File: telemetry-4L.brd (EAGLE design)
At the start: 69.8 x 22.9 mm, 70 parts, among them SW1 MF-SW-TACT-4.2MM, SW2 SWITCH_SPDT, U1 ATSAMD21G18A-MUT, U2 SPX3819M5-L-3-0, U3 MCP73831T-2ACI/OT, U4 DMG6968U, U5 SIM868, U6 BMP280, U7 MPU-9250, U8 TPS61253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

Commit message: Seems ok now
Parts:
- L1: value DFE322512C -> 1277AS-H-1R0M=P2
- SW2: value SWITCH_SPDT -> PCM12SMTR
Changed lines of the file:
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@@
 <layer number="25" name="tNames" color="7" fill="1" visible="yes" active="yes"/>
 <layer number="26" name="bNames" color="7" fill="1" visible="yes" active="yes"/>
-<layer number="27" name="tValues" color="7" fill="1" visible="no" active="yes"/>
-<layer number="28" name="bValues" color="7" fill="1" visible="no" active="yes"/>
+<layer number="27" name="tValues" color="7" fill="1" visible="yes" active="yes"/>
+<layer number="28" name="bValues" color="7" fill="1" visible="yes" active="yes"/>
 <layer number="29" name="tStop" color="7" fill="3" visible="yes" active="yes"/>
 <layer number="30" name="bStop" color="7" fill="6" visible="yes" active="yes"/>
@@
 <attribute name="VALUE" x="64.897" y="6.1595" size="0.889" layer="28" ratio="11" rot="MR180"/>
 </element>
-<element name="SW2" library="SparkFun-Electromechanical" package="KPS-1290" value="SWITCH_SPDT" x="1.778" y="11.43" rot="MR90">
+<element name="SW2" library="SparkFun-Electromechanical" package="KPS-1290" value="PCM12SMTR" x="1.778" y="11.43" rot="MR90">
 <attribute name="PROD_ID" value="SWCH-10651" x="1.778" y="11.43" size="1.778" layer="28" rot="MR90" display="off"/>
 </element>
@@
 <attribute name="VALUE" x="50.673" y="23.1775" size="1.27" layer="28" font="vector" ratio="18" rot="MR180" align="center"/>
 </element>
-<element name="L1" library="MF_Passives" package="L1210" value="DFE322512C" x="47.6885" y="20.3835" smashed="yes" rot="MR90">
+<element name="L1" library="MF_Passives" package="L1210" value="1277AS-H-1R0M=P2" x="47.6885" y="20.3835" smashed="yes" rot="MR90">
 <attribute name="HOUSEPART" value="" x="47.6885" y="20.3835" size="1.778" layer="28" rot="MR90" display="off"/>
 <attribute name="POPULATE" value="" x="47.6885" y="20.3835" size="1.778" layer="28" rot="MR90" display="off"/>

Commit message: fixed some names
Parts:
- U4: value DMG6968U -> IRLML6344TRPBF
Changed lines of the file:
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@@
 <element name="JP7" library="SparkFun-Passives" package="PAD-JUMPER-2-NO_YES_SILK" value="JUMPER-PAD-2-NOYES_SILK" x="4.572" y="7.62" rot="MR0"/>
 <element name="JP8" library="SparkFun-Passives" package="PAD-JUMPER-2-NC_BY_TRACE_YES_SILK" value="JUMPER-PAD-2-NC_BY_TRACE" x="4.572" y="15.24" rot="MR0"/>
-<element name="U4" library="MF_Discrete_Semiconductor" package="SOT-23-3" value="DMG6968U" x="66.421" y="16.002" smashed="yes" rot="R90">
+<element name="U4" library="MF_Discrete_Semiconductor" package="SOT-23-3" value="IRLML6344TRPBF" x="66.421" y="16.002" smashed="yes" rot="R90">
 <attribute name="MPN" value="" x="66.421" y="16.002" size="1.778" layer="27" rot="R90" display="off"/>
 <attribute name="HOUSEPART" value="NO" x="66.421" y="16.002" size="1.778" layer="27" rot="R90" display="off"/>

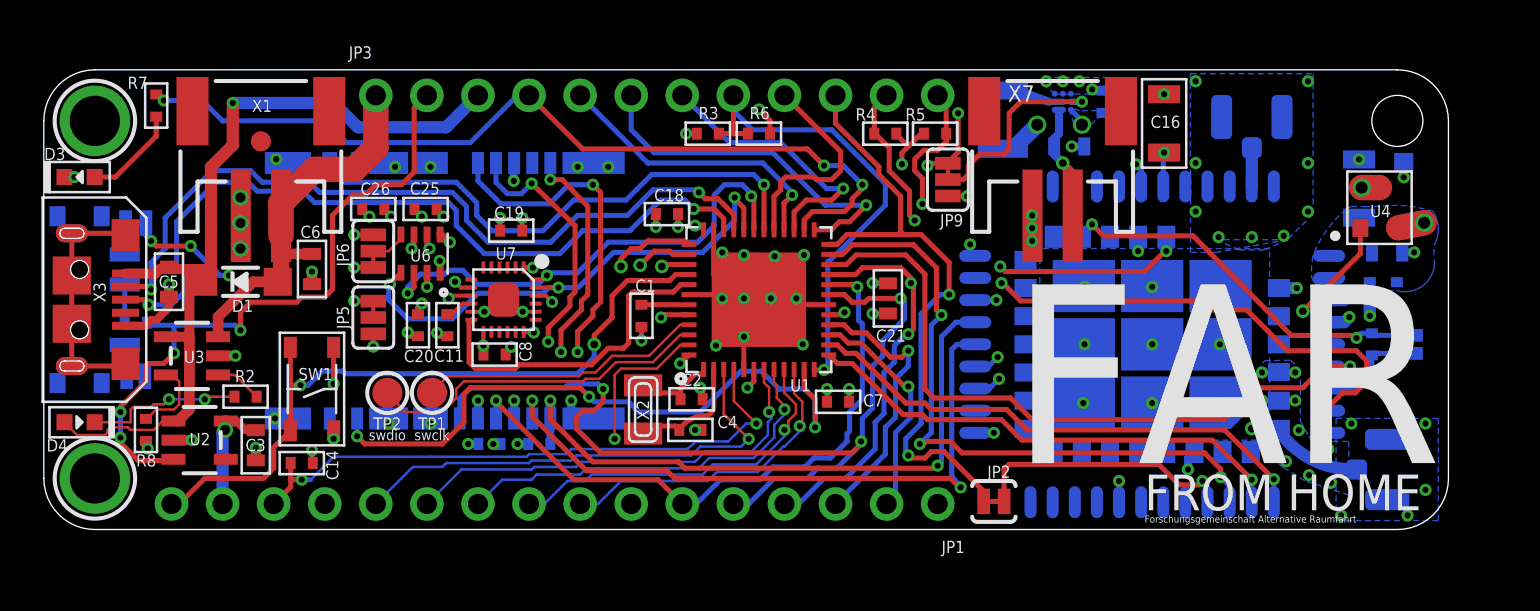
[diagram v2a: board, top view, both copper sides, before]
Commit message: Moved power mosfet back upstream
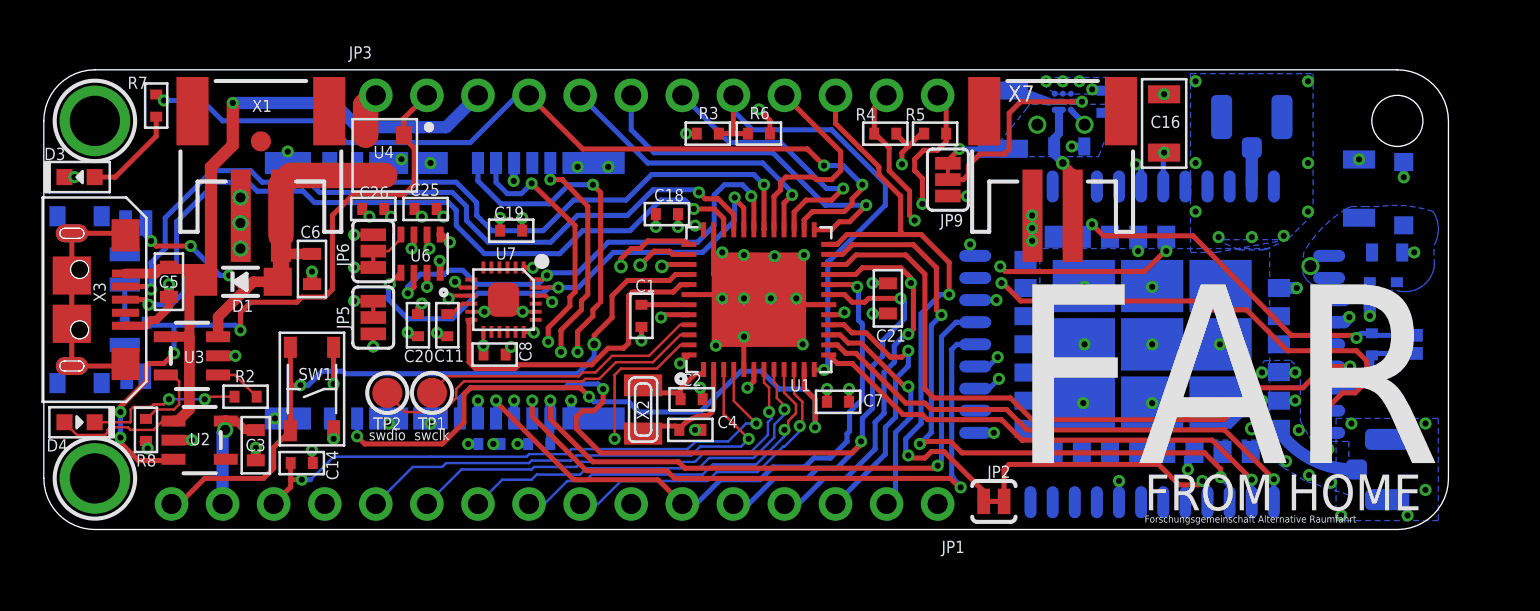
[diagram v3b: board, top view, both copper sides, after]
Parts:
- moved U4 49.5 mm to (17.0, 18.6), turned to 270 degrees
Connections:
- net EN: no longer JP9.3
- net VBAT: no longer C22.P$1, JP3.1, L1.P$1, R3.P$1, U8.A3
- net VBAT_ON: now also C22.P$1, JP3.1, JP9.3, L1.P$1, R3.P$1, U8.A3
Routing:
- net VBAT: track 92.0 -> 24.3 mm, vias 7 -> 3
- net EN: track 94.2 -> 34.7 mm, vias 7 -> 4
- net VBAT_ON: track 1.30 -> 58.0 mm, vias 1 -> 5
- net GND: track 70.5 -> 71.4 mm
- removed copper zone on layer 16, net VBAT

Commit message: tweaks
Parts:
- removed U$34: FIDUCIAL"", microbuilder:FIDUCIAL_1MM
- D3: value RED -> MF-LED-0603-RED
- D4: value GREEN -> MF-LED-0603-GREEN
- U8: value TPS61253 -> TPS61253YFFR
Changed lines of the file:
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@@
 <attribute name="VALUE" x="66.230496875" y="15.684503125" size="0.4064" layer="28" rot="MR90"/>
 </element>
-<element name="D3" library="MF_LEDs" package="LED0603" value="RED" x="1.778" y="17.526" smashed="yes">
+<element name="D3" library="MF_LEDs" package="LED0603" value="MF-LED-0603-RED" x="1.778" y="17.526" smashed="yes">
 <attribute name="MPN" value="MF-LED-0603-RED" x="1.778" y="17.526" size="1.778" layer="27" display="off"/>
 <attribute name="URL" value="https://factory.macrofab.com/part/MF-LED-0603-RED" x="1.778" y="17.526" size="1.778" layer="27" display="off"/>
@@
 <attribute name="NAME" x="0.0145" y="18.372" size="0.6096" layer="25" font="vector" ratio="18"/>
 </element>
-<element name="D4" library="MF_LEDs" package="LED0603" value="GREEN" x="1.778" y="5.334" smashed="yes" rot="R180">
+<element name="D4" library="MF_LEDs" package="LED0603" value="MF-LED-0603-GREEN" x="1.778" y="5.334" smashed="yes" rot="R180">
 <attribute name="MPN" value="MF-LED-0603-GREEN" x="1.778" y="5.334" size="1.778" layer="27" rot="R180" display="off"/>
 <attribute name="URL" value="https://factory.macrofab.com/part/MF-LED-0603-GREEN" x="1.778" y="5.334" size="1.778" layer="27" rot="R180" display="off"/>
@@
 <attribute name="BOM" value="EXCLUDE" x="2.54" y="2.54" size="1.778" layer="27" display="off"/>
 </element>
-<element name="U$34" library="microbuilder" package="FIDUCIAL_1MM" value="FIDUCIAL&quot;&quot;" x="10.795" y="19.304" smashed="yes">
-<attribute name="BOM" value="EXCLUDE" x="10.795" y="19.304" size="1.778" layer="27" display="off"/>
-</element>
 <element name="U1" library="microbuilder" package="TQFN48_7MM" value="ATSAMD21G18A-MUT" x="35.56" y="11.43" smashed="yes">
 <attribute name="NAME" x="38.1411375" y="7.4745" size="0.6096" layer="25" font="vector" ratio="18" rot="R180"/>
@@
 </element>
 <element name="X7" library="microbuilder" package="JSTPH2" value="S2B-PH-SM4-TB(LF)(SN)" x="50.165" y="19.304"/>
-<element name="U8" library="Custom" package="YFF9" value="TPS61253" x="50.673" y="21.2725" smashed="yes" rot="MR180">
+<element name="U8" library="Custom" package="YFF9" value="TPS61253YFFR" x="50.673" y="21.2725" smashed="yes" rot="MR180">
 <attribute name="COPYRIGHT" value="Copyright (C) 2015 Accelerated Designs. All rights reserved" x="50.673" y="21.2725" size="1.778" layer="28" rot="MR180" display="off"/>
 <attribute name="VENDOR" value="Texas Instruments" x="50.673" y="21.2725" size="1.778" layer="28" rot="MR180" display="off"/>
@@
 <vertex x="49.022" y="21.1455"/>
 </polygon>
-<wire x1="32.47" y1="19.685" x2="44.958" y2="18.3515" width="0" layer="19" extent="1-1"/>
 <wire x1="51.7525" y1="20.1295" x2="51.073" y2="20.8725" width="0.3048" layer="16"/>
+<wire x1="44.958" y1="18.3515" x2="32.47" y2="19.685" width="0" layer="19" extent="1-1"/>
 </signal>
 <signal name="N$9">

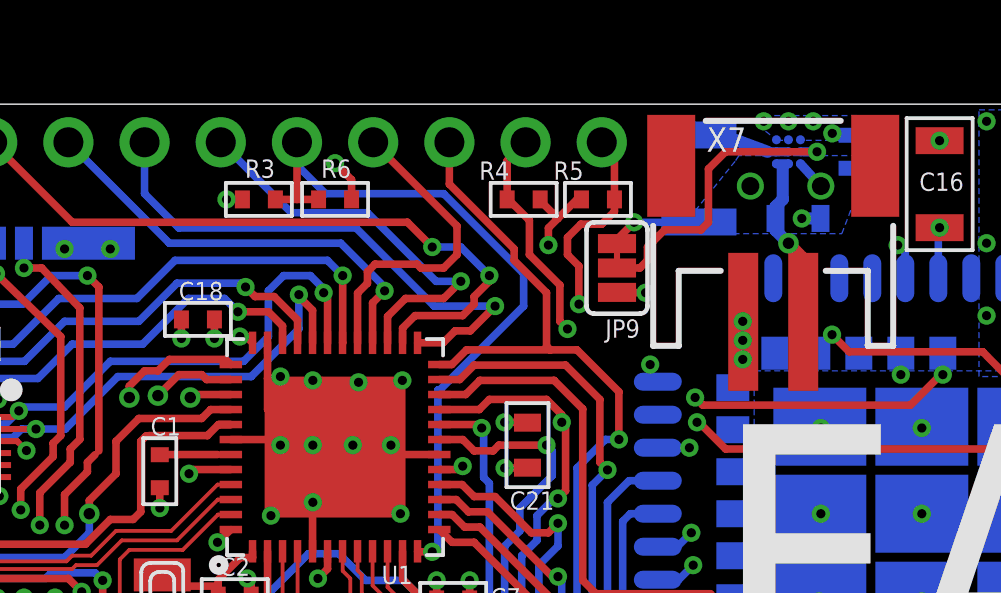
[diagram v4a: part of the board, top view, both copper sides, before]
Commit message: Changed GPS_EN pin to SERVO_EN, so I can arm at a distance
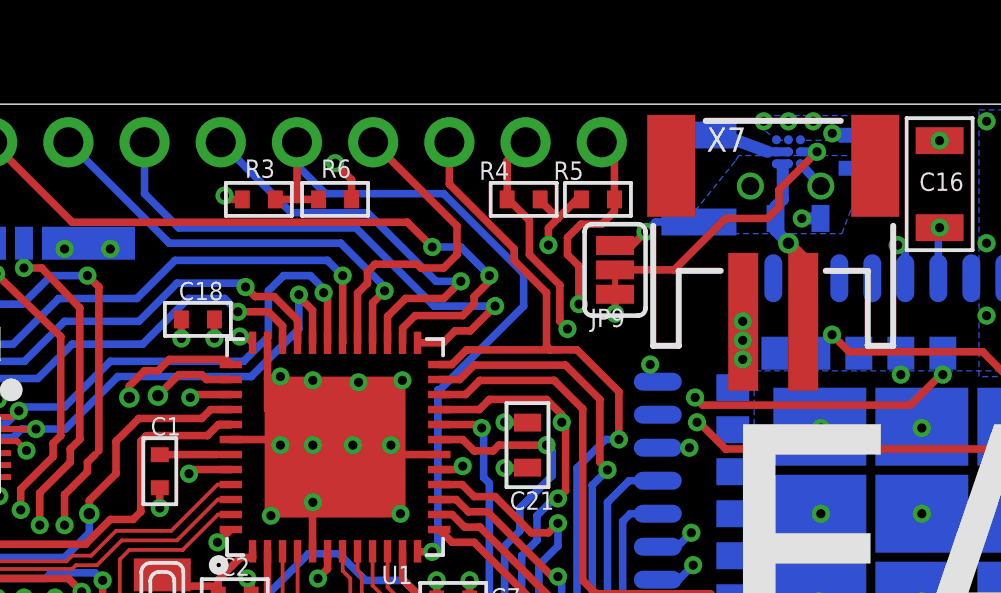
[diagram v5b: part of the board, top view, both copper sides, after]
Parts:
- moved JP9 0.09 mm to (44.9, 17.3), turned to 270 degrees
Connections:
- net N$9 renamed 5VSW
- removed net GPS_EN: JP4.1, R9.P$1, U1.39, U5.59_
- new net GPS_EN_: JP4.1, R9.P$1, U5.59_
- new net SERVO_EN: JP9.3, U1.39
- net GND: no longer JP9.1
- net VBAT_ON: now also JP9.1; no longer JP9.3
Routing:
- net GPS_EN: track 44.7 -> 0.00 mm, vias 3 -> 0
- net GPS_EN_: track 0.00 -> 19.2 mm, vias 0 -> 2
- net SERVO_EN: track 0.00 -> 17.5 mm, vias 0 -> 2
- net VBAT_ON: track 58.0 -> 59.2 mm
- net GND: track 71.4 -> 70.4 mm, vias 115 -> 114
- net 5V_EN: track 10.1 -> 9.25 mm
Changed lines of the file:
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@@
 <attribute name="NAME" x="52.535" y="18.4755" size="0.6096" layer="26" font="vector" ratio="18" rot="MR90"/>
 </element>
-<element name="JP9" library="SparkFun-Passives" package="PAD-JUMPER-3-2OF3_NC_BY_TRACE_YES_SILK_FULL_BOX" value="JUMPER-PAD-3-2OF3_NC_BY_TRACE_SMALL" x="44.958" y="17.399" smashed="yes" rot="R90">
-<attribute name="NAME" x="45.72" y="15.6845" size="0.6096" layer="25" font="vector" ratio="18" rot="R180"/>
-<attribute name="VALUE" x="46.863" y="16.129" size="0.4064" layer="27" rot="R90"/>
+<element name="JP9" library="SparkFun-Passives" package="PAD-JUMPER-3-2OF3_NC_BY_TRACE_YES_SILK_FULL_BOX" value="JUMPER-PAD-3-2OF3_NC_BY_TRACE_SMALL" x="44.8945" y="17.3355" smashed="yes" rot="R270">
+<attribute name="NAME" x="44.069" y="15.4305" size="0.6096" layer="25" font="vector" ratio="18"/>
+<attribute name="VALUE" x="42.9895" y="18.6055" size="0.4064" layer="27" rot="R270"/>
 </element>
 </elements>
@@
 <contactref element="U8" pad="C2"/>
 <contactref element="U8" pad="C3"/>
-<contactref element="JP9" pad="1"/>
 <contactref element="U8" pad="C1"/>
 <contactref element="X7" pad="1"/>
@@
 <wire x1="51.7405" y1="19.05" x2="51.1175" y2="19.05" width="0.4064" layer="16"/>
 <via x="51.1175" y="19.05" extent="1-16" drill="0.3048"/>
-<wire x1="44.958" y1="16.5862" x2="45.9105" y2="16.5735" width="0.254" layer="1"/>
-<via x="45.9105" y="16.5735" extent="1-16" drill="0.3048"/>
 <wire x1="64.9224" y1="11.6615" x2="64.6684" y2="11.4075" width="0.6096" layer="16"/>
 <wire x1="64.6684" y1="11.4075" x2="63.918" y2="11.4075" width="0.6096" layer="16"/>
@@
 <wire x1="53.848" y1="13.843" x2="54.418" y2="13.843" width="0.254" layer="15"/>
 </signal>
-<signal name="GPS_EN">
-<contactref element="U1" pad="39"/>
+<signal name="GPS_EN_">
 <contactref element="U5" pad="59_"/>
 <contactref element="JP4" pad="1"/>
@@
 <wire x1="65.278" y1="9.525" x2="65.5105" y2="9.7575" width="0.254" layer="16"/>
 <wire x1="65.5105" y1="9.7575" x2="66.04" y2="9.7575" width="0.254" layer="16"/>
-<wire x1="32.085" y1="13.18" x2="30.833" y2="13.18" width="0.254" layer="1"/>
-<wire x1="30.833" y1="13.18" x2="30.734" y2="13.081" width="0.254" layer="1"/>
-<via x="30.734" y="13.081" extent="1-16" drill="0.381"/>
-<wire x1="30.734" y1="13.081" x2="30.7975" y2="13.0175" width="0.254" layer="15"/>
-<wire x1="30.7975" y1="13.0175" x2="38.1635" y2="13.0175" width="0.254" layer="15"/>
-<wire x1="38.1635" y1="13.0175" x2="39.624" y2="14.478" width="0.254" layer="15"/>
-<wire x1="46.4185" y1="14.859" x2="47.0535" y2="14.224" width="0.254" layer="15"/>
-<wire x1="46.4185" y1="14.859" x2="45.5295" y2="14.859" width="0.254" layer="15"/>
-<wire x1="45.5295" y1="14.859" x2="45.1485" y2="14.478" width="0.254" layer="15"/>
-<wire x1="45.1485" y1="14.478" x2="39.624" y2="14.478" width="0.254" layer="15"/>
-<wire x1="47.0535" y1="14.224" x2="48.133" y2="14.224" width="0.254" layer="15"/>
-<wire x1="48.133" y1="14.224" x2="49.149" y2="13.208" width="0.254" layer="15"/>
-<wire x1="49.149" y1="13.208" x2="50.8635" y2="13.208" width="0.254" layer="15"/>
-<wire x1="50.8635" y1="13.208" x2="51.618" y2="13.9625" width="0.254" layer="15"/>
-<wire x1="51.618" y1="13.9625" x2="51.618" y2="14.6685" width="0.254" layer="15"/>
-<wire x1="51.618" y1="14.6685" x2="52.126" y2="15.1765" width="0.254" layer="15"/>
 </signal>
 <signal name="D4/TX2/GSM_RX">
@@
 <contactref element="U5" pad="34_"/>
 <via x="62.9895" y="13.097" extent="1-16" drill="0.6"/>
-<contactref element="JP9" pad="3"/>
 <contactref element="L1" pad="P$1"/>
 <contactref element="C22" pad="P$1"/>
@@
 <wire x1="49.403" y1="20.1295" x2="46.482" y2="20.1295" width="1.27" layer="15"/>
 <wire x1="46.482" y1="20.1295" x2="46.1645" y2="19.812" width="1.27" layer="15"/>
-<wire x1="46.1645" y1="19.812" x2="18.288" y2="19.812" width="1.27" layer="15"/>
+<wire x1="46.1645" y1="19.812" x2="31.877" y2="19.812" width="1.27" layer="15"/>
 <contactref element="R3" pad="P$1"/>
+<wire x1="31.877" y1="19.812" x2="18.288" y2="19.812" width="1.27" layer="15"/>
 <wire x1="32.4485" y1="19.6635" x2="32.47" y2="19.685" width="0.254" layer="1"/>
-<via x="31.9405" y="19.685" extent="1-16" drill="0.3048"/>
-<wire x1="31.9405" y1="19.685" x2="32.47" y2="19.685" width="0.254" layer="1"/>
 <contactref element="JP3" pad="1"/>
 <wire x1="16.0045" y1="19.6055" x2="16.0045" y2="21.0845" width="1.27" layer="1"/>
 <wire x1="16.0045" y1="21.0845" x2="16.51" y2="21.59" width="1.27" layer="1"/>
 <wire x1="16.51" y1="21.59" x2="18.288" y2="19.812" width="1.27" layer="15"/>
-<wire x1="44.958" y1="18.2118" x2="44.958" y2="18.3515" width="0.254" layer="1"/>
-<wire x1="44.958" y1="18.3515" x2="45.5295" y2="18.923" width="0.254" layer="1"/>
-<via x="45.5295" y="18.923" extent="1-16" drill="0.3048"/>
-<wire x1="45.5295" y1="18.923" x2="47.678" y2="18.923" width="0.254" layer="16"/>
 <wire x1="47.678" y1="18.923" x2="47.6885" y2="18.9335" width="0.254" layer="16"/>
 <via x="49.403" y="20.1295" extent="1-16" drill="0.6"/>
@@
 </polygon>
 <wire x1="51.7525" y1="20.1295" x2="51.073" y2="20.8725" width="0.3048" layer="16"/>
-<wire x1="44.958" y1="18.3515" x2="32.47" y2="19.685" width="0" layer="19" extent="1-1"/>
-</signal>
-<signal name="N$9">
+<contactref element="JP9" pad="1"/>
+<wire x1="32.47" y1="19.685" x2="32.004" y2="19.685" width="0.254" layer="1"/>
+<wire x1="32.004" y1="19.685" x2="31.877" y2="19.812" width="0.254" layer="1"/>
+<via x="31.877" y="19.812" extent="1-16" drill="0.3048"/>
+<via x="45.9105" y="18.6055" extent="1-16" drill="0.3048"/>
+<wire x1="47.572" y1="19.05" x2="47.6885" y2="18.9335" width="0.254" layer="16"/>
+<wire x1="46.7465" y1="18.9335" x2="47.6885" y2="18.9335" width="0.254" layer="16"/>
+<wire x1="45.9105" y1="18.6055" x2="45.4533" y2="18.1483" width="0.254" layer="1"/>
+<wire x1="45.4533" y1="18.1483" x2="44.8945" y2="18.1483" width="0.254" layer="1"/>
+<wire x1="45.9105" y1="18.6055" x2="46.2385" y2="18.9335" width="0.254" layer="16"/>
+<wire x1="46.2385" y1="18.9335" x2="47.6885" y2="18.9335" width="0.254" layer="16"/>
+</signal>
+<signal name="5VSW">
 <contactref element="U8" pad="B1"/>
 <contactref element="L1" pad="P$2"/>
@@
 <signal name="5V_EN">
 <contactref element="U8" pad="B3"/>
-<contactref element="JP9" pad="2"/>
 <wire x1="51.073" y1="21.2725" x2="51.6255" y2="21.2725" width="0.3048" layer="16"/>
 <via x="51.6255" y="21.2725" extent="1-16" drill="0.3048"/>
-<wire x1="51.6255" y1="21.2725" x2="48.5775" y2="21.2725" width="0.254" layer="1"/>
-<wire x1="48.5775" y1="21.2725" x2="48.006" y2="20.701" width="0.254" layer="1"/>
-<wire x1="48.006" y1="20.701" x2="48.006" y2="18.923" width="0.254" layer="1"/>
-<wire x1="48.006" y1="18.923" x2="47.752" y2="18.669" width="0.254" layer="1"/>
-<wire x1="47.752" y1="18.669" x2="46.5455" y2="18.669" width="0.254" layer="1"/>
-<wire x1="46.5455" y1="18.669" x2="45.974" y2="18.0975" width="0.254" layer="1"/>
-<wire x1="45.974" y1="18.0975" x2="45.974" y2="17.653" width="0.254" layer="1"/>
-<wire x1="45.974" y1="17.653" x2="45.72" y2="17.399" width="0.254" layer="1"/>
-<wire x1="45.72" y1="17.399" x2="44.958" y2="17.399" width="0.254" layer="1"/>
+<wire x1="48.5775" y1="19.05" x2="46.863" y2="17.3355" width="0.254" layer="1"/>
+<contactref element="JP9" pad="2"/>
+<wire x1="46.863" y1="17.3355" x2="44.8945" y2="17.3355" width="0.254" layer="1"/>
+<wire x1="51.6255" y1="21.2725" x2="50.3555" y2="20.0025" width="0.254" layer="1"/>
+<wire x1="50.3555" y1="20.0025" x2="50.3555" y2="19.431" width="0.254" layer="1"/>
+<wire x1="50.3555" y1="19.431" x2="49.9745" y2="19.05" width="0.254" layer="1"/>
+<wire x1="49.9745" y1="19.05" x2="48.5775" y2="19.05" width="0.254" layer="1"/>
+</signal>
+<signal name="SERVO_EN">
+<contactref element="U1" pad="39"/>
+<contactref element="JP9" pad="3"/>
+<wire x1="32.085" y1="13.18" x2="30.833" y2="13.18" width="0.254" layer="1"/>
+<wire x1="30.833" y1="13.18" x2="30.734" y2="13.081" width="0.254" layer="1"/>
+<via x="30.734" y="13.081" extent="1-16" drill="0.3048"/>
+<wire x1="38.1" y1="12.954" x2="39.624" y2="14.478" width="0.254" layer="15"/>
+<wire x1="39.624" y1="14.478" x2="43.4975" y2="14.478" width="0.254" layer="15"/>
+<wire x1="43.4975" y1="14.478" x2="44.8945" y2="15.875" width="0.254" layer="15"/>
+<via x="44.8945" y="15.875" extent="1-16" drill="0.3048"/>
+<wire x1="44.8945" y1="15.875" x2="44.8945" y2="16.5227" width="0.254" layer="1"/>
+<wire x1="30.734" y1="13.081" x2="30.861" y2="12.954" width="0.254" layer="15"/>
+<wire x1="30.861" y1="12.954" x2="38.1" y2="12.954" width="0.254" layer="15"/>
 </signal>
 </signals>
